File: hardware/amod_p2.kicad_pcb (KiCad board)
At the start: 4 copper layers, 100 x 100 mm, 84 parts, among them J1401 SMA, J1402 SMA, J1403 SMA, J1404 SMA, J1405 SMA, J1406 SMA, J1501 SMA, J1502 SMA, J1601 SMA, J1602 SMA, J1603 SMA, J1701 SMA, J1702 SMA, J1703 SMA, J1801 SMA, J1802 SMA, J1901 SMA, J1902 SMA, J2001 SMA, J2002 SMA, J2101 SMA, J2102 SMA, J2201 SMA, J2202 SMA, J2203 Pmod, J2301 SMA, J2302 SMA, J2401 SMA, J2402 SMA, J2501 SMA, J2502 SMA, Q2301 AO3401A, Q2302 MMBT3904, SW2301 ON, SW2501 LOAD, T2401 TC1-1TG2+, T2501 TC4-1W+, U1701 ADP-2-1+, U2201 PE43711

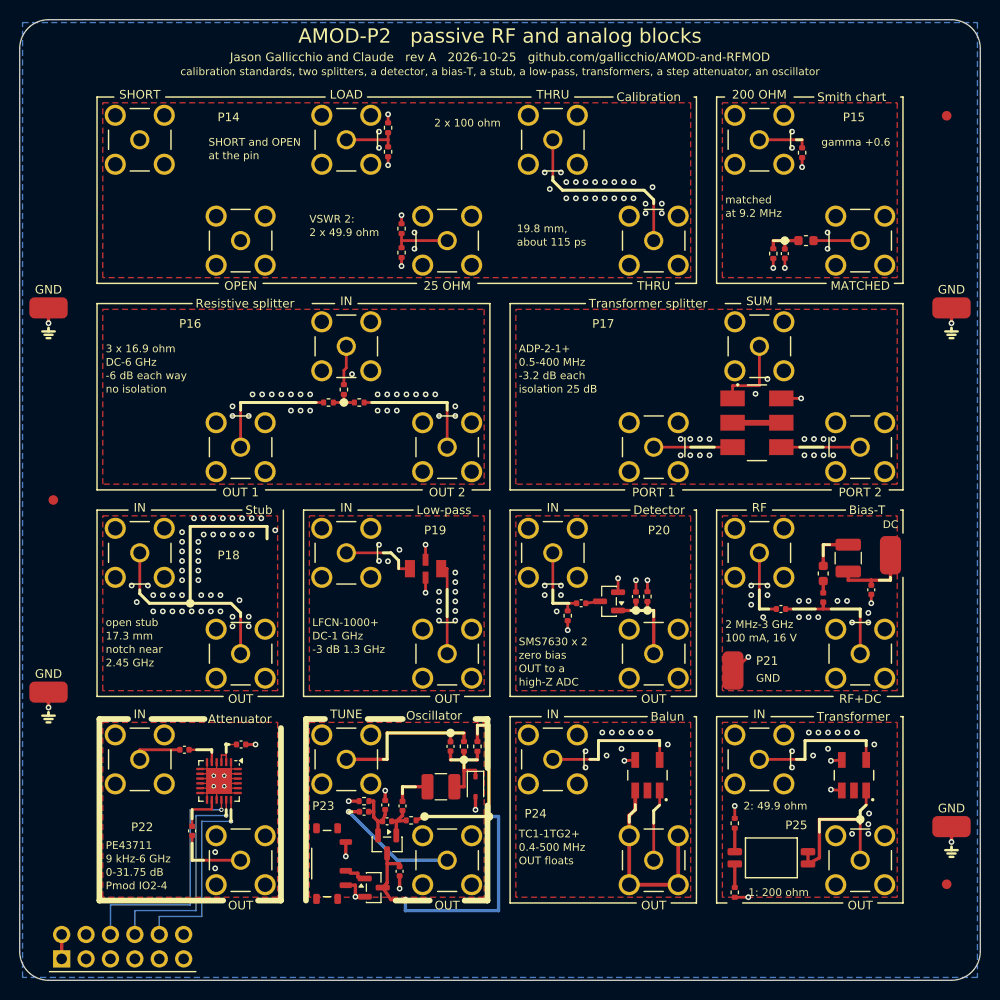
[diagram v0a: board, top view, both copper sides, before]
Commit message: Back-side panels on all six boards; P22 set by hand or by the FPGA; P15 dropped
Jason, Prompt 18: "I hope that the silkscreen (including on the back) is appropriately used to document anything that a
user definitely needs to know to use the tiles successfully and without damaging anything.  If there is additional room
on the back, putting plots of expected responses or other relevant parameters would be great."

- gen_pcb.back_panels: under each tile, mirrored on the back silk, its number and title and the lines in its board's
  BACK dict (levels, loads, supplies, cautions), and where there is one its expected response as a small plot
  (BACK_PLOTS, or the ladder tiles' own simulation; scripts/backplots.py for the rest: amplifiers, datasheet tables,
  the open stub, P23's tuning curve, P10's clipping curve).  A panel goes as one block or in two to four parts, each
  below the one before, clear of the back's tracks and vias where it can be; every panel and plot placed, DRC 0.
- Front silk: Y2 says PULSES ONLY, Y10 "start at mV", R5 and X4 their input level (IN -20 dBm) in place of the noise
  figure.
- P22 (PE43711) on two cells with an 8-way DIP switch: way 1 SPI, ways 2-8 the bits (direct parallel mode with LE pulled
  high), 100 k pull-downs; it still needs the Pmod's 3.3 V.  P15 (two Smith-chart loads) dropped for the cell; P23 moved
  to (3,0).

Co-Authored-By: Claude Opus 5.5 <noreply@anthropic.com>
Claude-Session: https://claude.ai/code/session_01RKeoKvFFzjk3cEBLCXXHnB
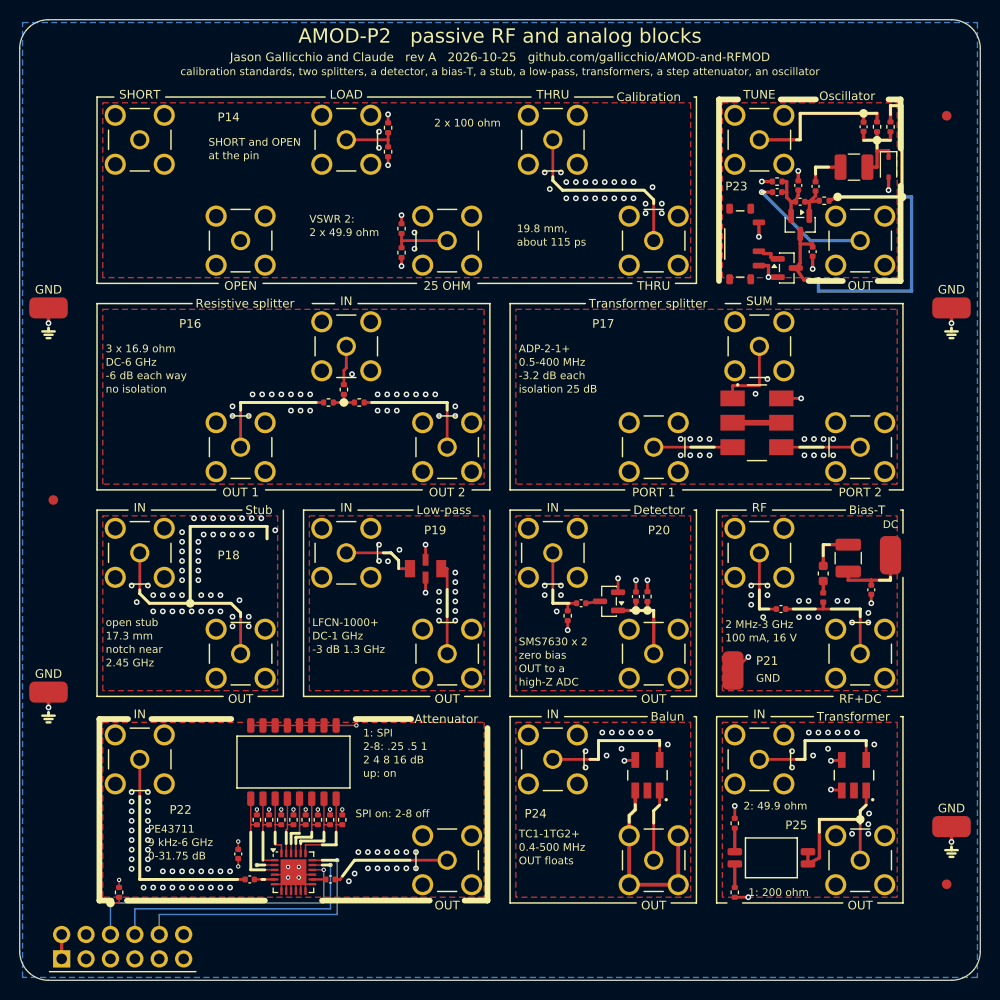
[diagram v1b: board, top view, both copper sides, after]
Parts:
- removed C1501: 150p, Capacitor_SMD:C_0402_1005Metric
- removed J1501, J1502: SMA, amod:SMA_BWSMA-KE-Z001_Vertical
- removed L1501: 1.5u, Inductor_SMD:L_0603_1608Metric
- removed R1501, R1502: 200, Resistor_SMD:R_0402_1005Metric
- added R2201: 100k, Resistor_SMD:R_0402_1005Metric, F.Cu at (24.7, 83.3)
- added R2202: 100k, Resistor_SMD:R_0402_1005Metric, F.Cu at (26.0, 83.3)
- added R2203: 100k, Resistor_SMD:R_0402_1005Metric, F.Cu at (27.2, 83.3)
- added R2204: 100k, Resistor_SMD:R_0402_1005Metric, F.Cu at (28.5, 83.3)
- added R2205: 100k, Resistor_SMD:R_0402_1005Metric, F.Cu at (29.8, 83.3)
- added R2206: 100k, Resistor_SMD:R_0402_1005Metric, F.Cu at (31.0, 83.3)
- added R2207: 100k, Resistor_SMD:R_0402_1005Metric, F.Cu at (32.3, 83.3)
- added R2208: 100k, Resistor_SMD:R_0402_1005Metric, F.Cu at (33.6, 83.3)
- added R2209: 100k, Resistor_SMD:R_0402_1005Metric, F.Cu at (10.3, 90.8)
- added SW2201: SPI / dB, amod:SW_DIP_SPSTx08_Slide_1.27mm_DSHP08, F.Cu at (28.5, 77.3)
- moved C2301 77.5 mm to (81.2, 18.9)
- moved C2302 77.5 mm to (81.0, 17.2)
- moved C2306 77.5 mm to (82.5, 24.1)
- moved D2301 77.5 mm to (90.5, 15.3)
- moved J2301 77.5 mm to (77.0, 12.5)
- moved J2302 77.5 mm to (87.5, 23.0)
- moved Q2302 77.5 mm to (81.2, 21.4)
- moved R2302 77.5 mm to (83.8, 18.9)
- moved R2303 77.5 mm to (89.2, 11.2)
- moved R2304 77.5 mm to (90.7, 11.2)
- moved SW2301 77.5 mm to (75.0, 23.4)
- moved C2303 77.5 mm to (78.8, 17.9)
- moved C2304 77.5 mm to (82.8, 17.4)
- moved C2305 77.5 mm to (87.8, 11.2)
- moved L2301 77.5 mm to (86.8, 15.3)
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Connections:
- C2201 pad 1: /P22_IN -> /PMOD_VCC
- C2201 pad 2: /P22_RA -> GND
- C2202 pad 1: /P22_OUT -> /P22_IN
- C2202 pad 2: /P22_RB -> /P22_RA
- C2203 pad 1: /PMOD_VCC -> /P22_RB
- C2203 pad 2: GND -> /P22_OUT
- U2201 pad 1: GND -> /P22_B0
- U2201 pad 19: GND -> /P22_B6
- U2201 pad 20: GND -> /P22_B5
- U2201 pad 21: GND -> /P22_B4
- U2201 pad 22: GND -> /P22_B3
- U2201 pad 23: GND -> /P22_B2
- U2201 pad 24: GND -> /P22_B1
- U2201 pad 3: /PMOD_VCC -> /P22_PS
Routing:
- net /P22_IN: track 5.17 -> 23.5 mm
- net /P22_PS: track 0.00 -> 10.5 mm
- net /PMOD_VCC: track 9.85 -> 20.2 mm, vias 2 -> 5
- net /P22_B6: track 0.00 -> 9.53 mm
- net /P22_B5: track 0.00 -> 8.76 mm
- net /P22_B0: track 0.00 -> 8.26 mm
- net /P22_B4: track 0.00 -> 7.99 mm
- net /PMOD2: track 21.5 -> 28.8 mm
- net /P22_B3: track 0.00 -> 7.22 mm
- net /P22_B1: track 0.00 -> 6.99 mm
- net /P22_B2: track 0.00 -> 6.45 mm
- net /PMOD4: track 25.6 -> 31.6 mm, vias 1 -> 2
- net /PMOD3: track 23.5 -> 29.5 mm
- net /P15_RA: track 5.29 -> 0.00 mm
- net /P22_OUT: track 7.62 -> 12.7 mm
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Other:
- board text added: "+2V"
- board text added: "-2V"
- board text added: "-3.2 dB each way"
- board text added: "-30 dB 1.9-5 G"
- board text added: "0 to -40 dB"
- board text added: "0 to -60 dB"
- board text added: "0.1G"
- board text added: "0.25 W, 30 mA"
- board text added: "100 mA max"
- board text added: "10M"
- board text added: "12 to 9 MHz"
- board text added: "1: 200, 2: 49.9"
- board text added: "1: SPI"
- board text added: "2 4 8 16 dB"
- board text added: "2-8: .25 .5 1"
- board text added: "25 OHM: VSWR 2"
- board text added: "3-800 MHz"
- board text added: "400M"
- board text added: "4x the Z"
- board text added: "5.5G"
- board text added: "50 ohm"
- board text added: "500k"
- board text added: "6G"
- board text added: "DC 16 V max"
- board text added: "FPGA: bits off, SPI on"
- board text added: "HIGH-Z ADC"
- board text added: "IN < +10 dBm"
- board text added: "IN max +20 dBm"
- board text added: "IN max +23 dBm, +9.5 dBm"
- board text added: "LOAD at the pin"
- board text added: "NEEDS THE PMOD'S 3.3 V"
- board text added: "OUT -22 dBm"
- board text added: "OUT: 2x V,"
- board text added: "P14 Calibration"
- board text added: "P16 Resistive splitter"
- board text added: "P17 Transformer splitter"
- board text added: "P18 Stub"
- board text added: "P19 Low-pass"
- board text added: "P20 Detector"
- board text added: "P21 Bias-T"
- board text added: "P22 Attenuator"
- board text added: "P23 Oscillator"
- board text added: "P24 Balun"
- board text added: "P25 Transformer"
- board text added: "Pmod 3.3 V"
- board text added: "RF+DC has DC:"
- board text added: "SHORT, OPEN,"
- board text added: "SPI on: 2-8 off"
- board text added: "THRU 115 ps"
- board text added: "TUNE +-2 V"
- board text added: "a combiner too"
- board text added: "and 7.35 GHz"
- board text added: "below -20 dBm"
- board text added: "below 0.5 MHz"
- board text added: "by hand: SPI off, bits on"
- board text added: "from their pads"
- board text added: "isolation 0 to -40 dB"
- board text added: "mind its load"
- board text added: "notch 2.45 GHz"
- board text added: "slide up: on"
- board text added: "square law"
- board text added: "tiles measure"
- board text added: "up: on"
- board text removed: "200 OHM"
- board text removed: "MATCHED"
- board text removed: "P15"
- board text removed: "Pmod IO2-4"
- board text removed: "Smith chart"
- board text removed: "at 9.2 MHz"
- board text removed: "gamma +0.6"
- board text removed: "matched"
